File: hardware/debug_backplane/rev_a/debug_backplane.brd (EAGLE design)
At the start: 177.8 x 177.8 mm, 297 parts, among them IC3 FT232RQ, J0 BACKPLANE_GENERIC_MODULE_DEBUG, J1 BACKPLANE_GENERIC_MODULE_DEBUG, J2 PJ-102AH, J3 BACKPLANE_CONTROLLER_MODULE_D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, J4 MICRO_USB_B_HIROSE_ZX62-B-5PA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, J5 MICRO_USB_B_HIROSE_ZX62-B-5PA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, J6 MICRO_USB_B_HIROSE_ZX62-B-5PA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, J8 MICRO_USB_B_HIROSE_ZX62-B-5PA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, J9 MICRO_USB_B_HIROSE_ZX62-B-5PA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, Q1 MOSFET-NCHANNELSMD, Q2 MOSFET-NCHANNELSMD, Q3 MOSFET-NCHANNELSMD, Q4 MOSFET-NCHANNELSMD, Q5 MOSFET-NCHANNELSMD, Q6 MOSFET-NCHANNELSMD, Q7 MOSFET-NCHANNELSMD, Q8 MOSFET-NCHANNELSMD, U1 TUSB2077A, U10 SAM4LC8AA, U11 LTC2941, U12 LTC2941, U13 FT232RQ, U14 SN74LVC2T45, U15 SN74LVC2T45, U16 FT232RQ, U2 FXMA2102, U20 TS3USB30E, U21 TS3USB30E, U26 MCP23008QFN, U27 MCP23008QFN, U3 FXMA2102, U4 MAX8887EZK33+T, U40 FT232RQ, U41 FT232RQ, U5 LTC2941, U6 PCA9544AQFN-N20, U7 LTC2941, U8 SN74LVC2T45, U9 SN74LVC2T45, X1 16MHz, Y1 ABMM

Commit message: added correct usb headers
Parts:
- moved TP17 179.7 mm to (67.4, 44.2)
- moved TP25 172.7 mm to (72.9, 43.8)
- moved TP22 169.9 mm to (67.6, 45.7)
- moved TP26 166.0 mm to (70.6, 44.7)
- moved TP23 165.5 mm to (67.3, 45.7)
- moved TP24 159.7 mm to (65.3, 45.7)
- moved TP27 157.5 mm to (66.5, 46.4)
- moved TP4 109.8 mm to (64.9, 49.9)
- moved TP35 100.3 mm to (68.2, 46.4)
- moved TP34 92.7 mm to (68.5, 47.6)
- moved LOGO2 52.6 mm to (25.8, 144.4)
- moved R27 5.85 mm to (60.7, 46.1)
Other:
- board text removed: "!OVR !CUR2"
- board text removed: "VCC Cont"
- board text removed: "VCC Linux"

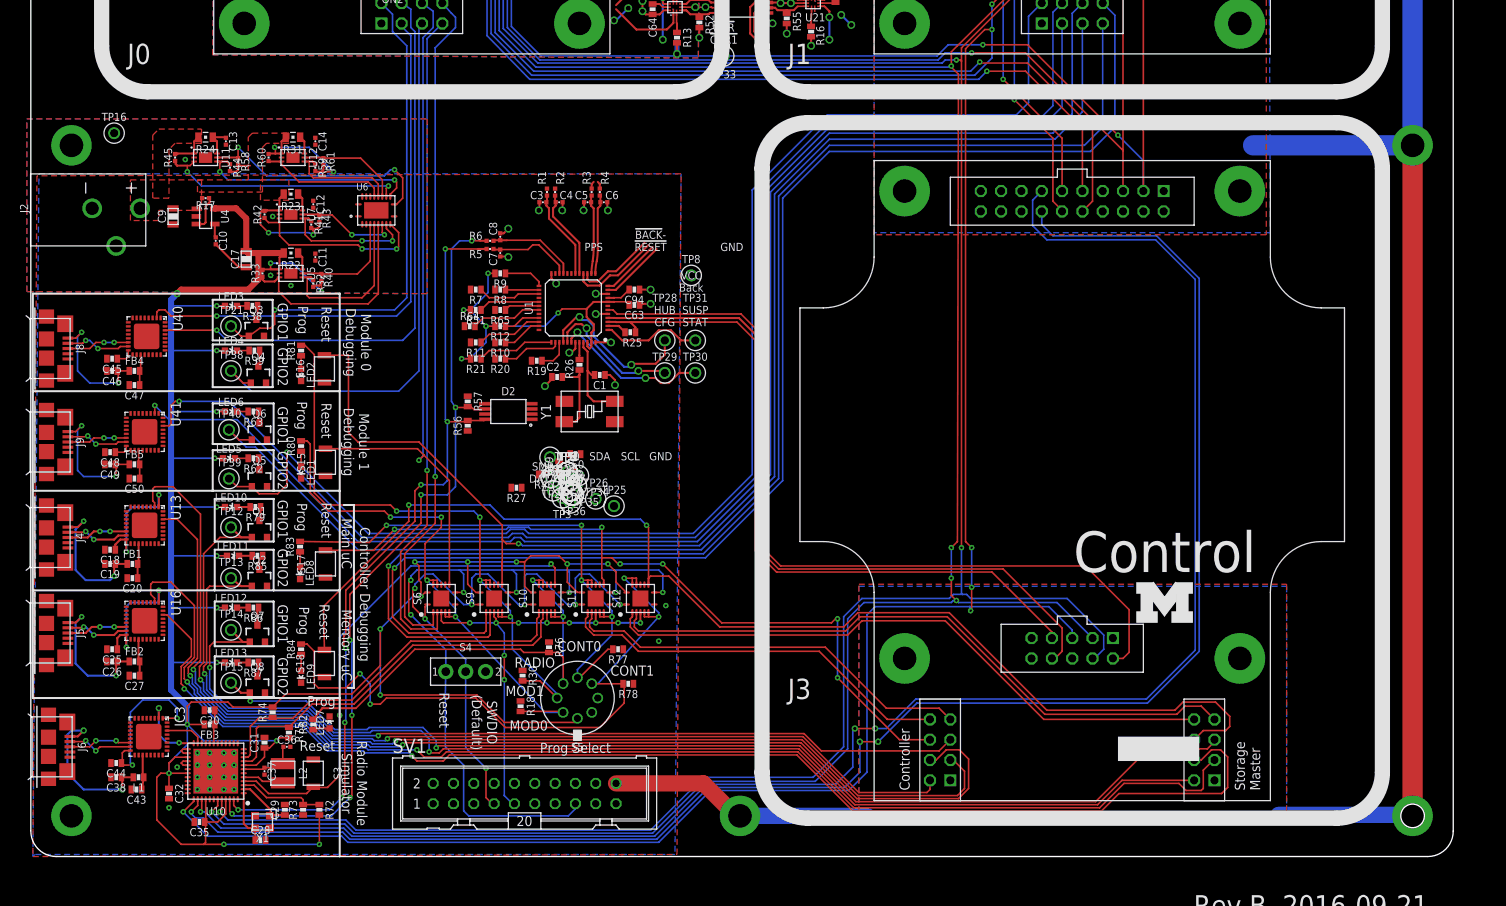
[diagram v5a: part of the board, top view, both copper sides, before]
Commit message: added usb switch circuit
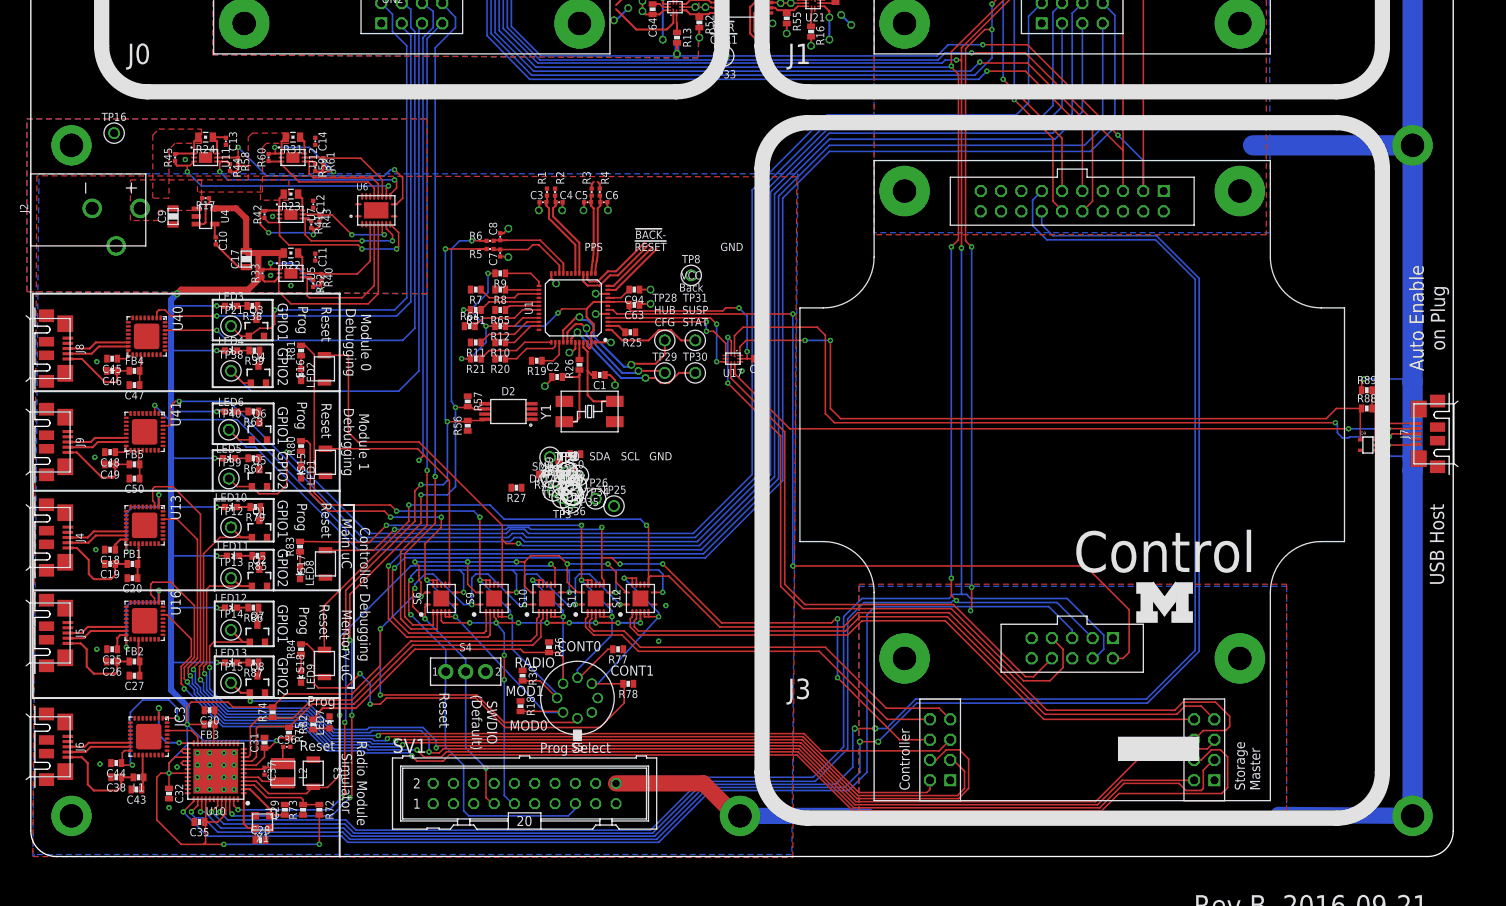
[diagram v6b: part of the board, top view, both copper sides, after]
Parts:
- added C55: 100nF, passives:0603_CAP
- added J7: MICRO_USB_B_HIROSE_ZX62R-B-5P, connector:USB_MICRO_B-HIROSE-ZX62R-B-5P
- added Q9: DMN32D2LDF, fets:SOT353
- added R88, R89: 100k, passives:0603-RES
- added U17: TS3USB30E, signpost:UQFN-10
- J4, J5, J6, J8, J9: value MICRO_USB_B_HIROSE_ZX62-B-5PA(11) -> MICRO_USB_B_HIROSE_ZX62R-B-5P; device connector:USB_MICRO_B-HIROSE-ZX62-B-5PA(11) -> connector:USB_MICRO_B-HIROSE-ZX62R-B-5P
- moved J6 0.25 mm to (0.51, 13.7)
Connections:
- new net N$25: J7.1, Q9.G2, R88.2, R89.2
- new net N$33: Q9.D2, R88.1, U17.10
- new net N$66: J7.3, U17.1
- new net N$81: J7.2, U17.7
- new net USB+: R25.1, U1.3, U17.3
- new net USB-: U1.4, U17.5
- net CONT_USB+: now also U17.2; no longer R25.1, U1.3
- net CONT_USB-: now also U17.6; no longer U1.4
- net GND: now also C55.1, J7.5, Q9.S, R89.1, U17.4, U17.8
- net VCC_BACKPLANE: now also C55.2, U17.9
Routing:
- net N$66: track 0.00 -> 100.1 mm, vias 0 -> 2
- net N$33: track 0.00 -> 92.7 mm, vias 0 -> 2
- net N$81: track 0.00 -> 89.2 mm, vias 0 -> 2
- net CONT_USB-: track 92.9 -> 69.4 mm
- net VCC_BACKPLANE: track 90.1 -> 113.1 mm, vias 18 -> 20
- net USB-: track 0.00 -> 19.8 mm, vias 0 -> 2
- net GND: track 542.5 -> 561.6 mm, vias 123 -> 131
- net USB+: track 0.00 -> 18.0 mm, vias 0 -> 2
- net N$25: track 0.00 -> 13.2 mm
- net CONT_USB+: track 89.3 -> 81.1 mm, vias 0 -> 2
- net N$46: track 20.1 -> 12.8 mm, vias 2 -> 0
- net N$37: track 16.5 -> 10.5 mm, vias 2 -> 0
- net N$22: track 17.4 -> 11.7 mm, vias 2 -> 0
- net N$30: track 15.8 -> 10.3 mm, vias 2 -> 0
- net N$64: track 17.2 -> 11.9 mm, vias 2 -> 0
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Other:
- board text added: "Auto Enable on Plug"
- board text added: "USB Host"

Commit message: fixed debug backplane schematic, vtref problem, usb problem
also checked usb spacing and lined them up with the board
also added power supply loops
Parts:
- removed LOGO2, LOGO3: UMICH_SOLID_MEDIUM, logos:UMICH_SOLID_200MIL
- added TP18, TP19: TEST_POINT_0.040IN, headers:TESTPOINT_0.040IN
- moved TP32 89.4 mm to (67.1, 47.6)
- moved SV1 2.16 mm to (59.6, 7.87)
- moved J6 0.72 mm to (0.00, 14.2)
- moved J8 0.57 mm to (0.00, 63.8)
- moved J4 0.51 mm to (0.00, 39.9)
- moved J5 0.51 mm to (0.00, 27.9)
- moved J9 0.51 mm to (0.00, 51.8)
- moved R83 0.13 mm to (33.7, 38.6)
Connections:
- net 3V3: now also S10.10, S11.10, S12.10
- net 5V: now also TP18.TESTPOINT
- net GND: now also TP19.TESTPOINT
- net JTAG_VTREF: now also S10.11, S11.11, S12.11, S6.11, S9.11
- net MOD0_VCCIO: now also S6.10
- net MOD1_VCCIO: now also S9.10
- net N$25: no longer R88.2
- net VCC_BACKPLANE: now also R88.2
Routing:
- net JTAG_VTREF: track 0.00 -> 78.9 mm, vias 0 -> 7
- net 3V3: track 358.2 -> 368.1 mm, vias 24 -> 27
- net RADIO_!RESET: track 64.0 -> 68.4 mm
- net CONT1_!RESET: track 150.4 -> 154.2 mm
- net N$25: track 13.2 -> 10.3 mm
- net PROG3_EN: track 69.2 -> 72.1 mm
- net CONT0_!RESET: track 98.4 -> 101.0 mm
- net JTAG_!RESET: track 98.8 -> 96.5 mm
- net GND: track 561.6 -> 563.7 mm
- net MOD1_DBG_TX: track 175.5 -> 173.4 mm
- net MOD1_DBG_RX: track 177.8 -> 175.7 mm
- net MOD1_DBG_GPIO1: track 166.2 -> 164.3 mm
- net MOD0_DBG_SWDIO: track 85.5 -> 87.3 mm
- net MOD1_DBG_GPIO2: track 170.7 -> 169.2 mm
- net MOD1_DBG_SWDIO: track 170.9 -> 172.3 mm
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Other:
- board text added: "MAIN"
- board text added: "MEM"
- board text removed: "!PWR !ON1"
- board text removed: "CONT0"
- board text removed: "CONT1"

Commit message: more routing
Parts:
- moved TP33 56.5 mm to (66.0, 47.5)
- moved C3 4.76 mm to (68.7, 81.0)
- moved C4 4.76 mm to (70.7, 81.0)
- moved R1 4.76 mm to (69.2, 82.3)
- moved R2 4.76 mm to (70.2, 82.3)
- moved C5 3.64 mm to (73.2, 81.0)
- moved C6 3.64 mm to (75.2, 81.0)
- moved R3 3.64 mm to (73.7, 82.3)
- moved R4 3.64 mm to (74.7, 82.3)
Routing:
- net MOD1_VCCIO: track 53.6 -> 247.1 mm, vias 4 -> 6
- net MOD0_VCCIO: track 55.6 -> 145.7 mm, vias 4 -> 6
- net MOD0_USB+: track 9.88 -> 96.8 mm, vias 0 -> 2
- net MOD0_USB-: track 9.69 -> 94.0 mm, vias 0 -> 2
- net HUB_!PWRON2: track 9.97 -> 93.0 mm, vias 0 -> 2
- net MOD1_USB+: track 2.69 -> 84.8 mm, vias 0 -> 2
- net MOD1_USB-: track 0.00 -> 81.3 mm, vias 0 -> 2
- net HUB_!OVRCUR2: track 15.0 -> 90.9 mm, vias 0 -> 2
- net MOD0_D-_HUB-SW: track 5.53 -> 48.8 mm
- net MOD0_D+_HUB-SW: track 5.47 -> 47.4 mm
- net MOD1_D-_HUB-SW: track 13.2 -> 44.0 mm
- net MOD1_D+_HUB-SW: track 15.0 -> 45.5 mm
- net MOD0_5V_METERED: track 58.7 -> 88.6 mm
- net GND: track 563.7 -> 582.3 mm
- net MOD1_USB_!EN: track 12.4 -> 7.50 mm, vias 4 -> 2
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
